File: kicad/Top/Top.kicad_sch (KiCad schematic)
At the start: 0 parts

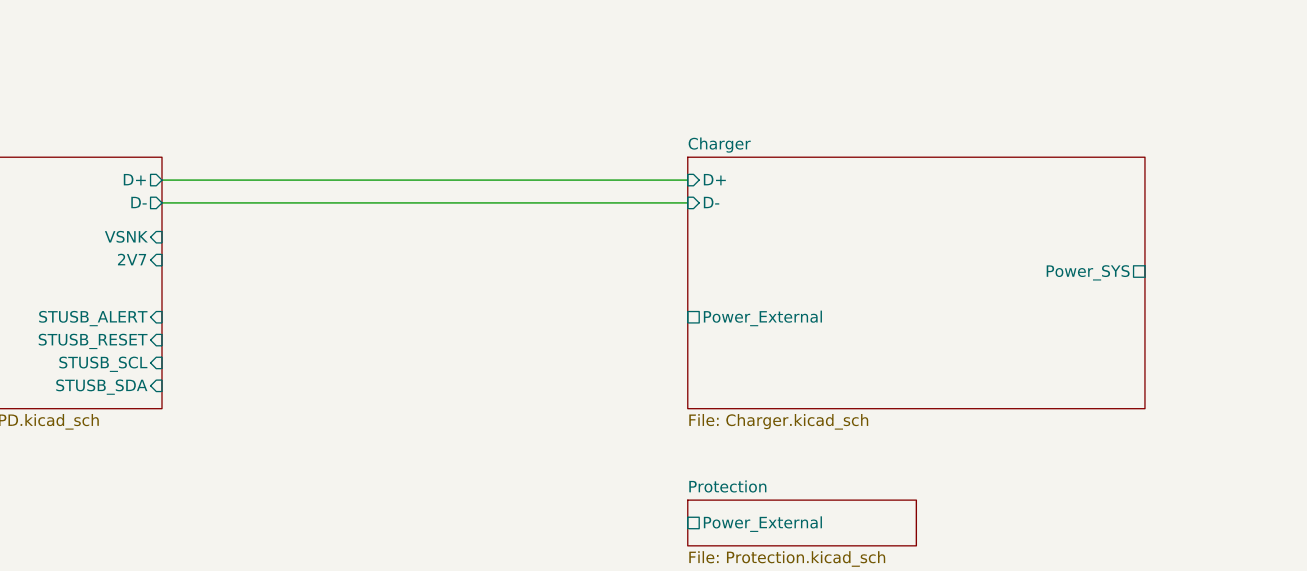
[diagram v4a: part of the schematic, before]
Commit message: Updated sheet pins for charger
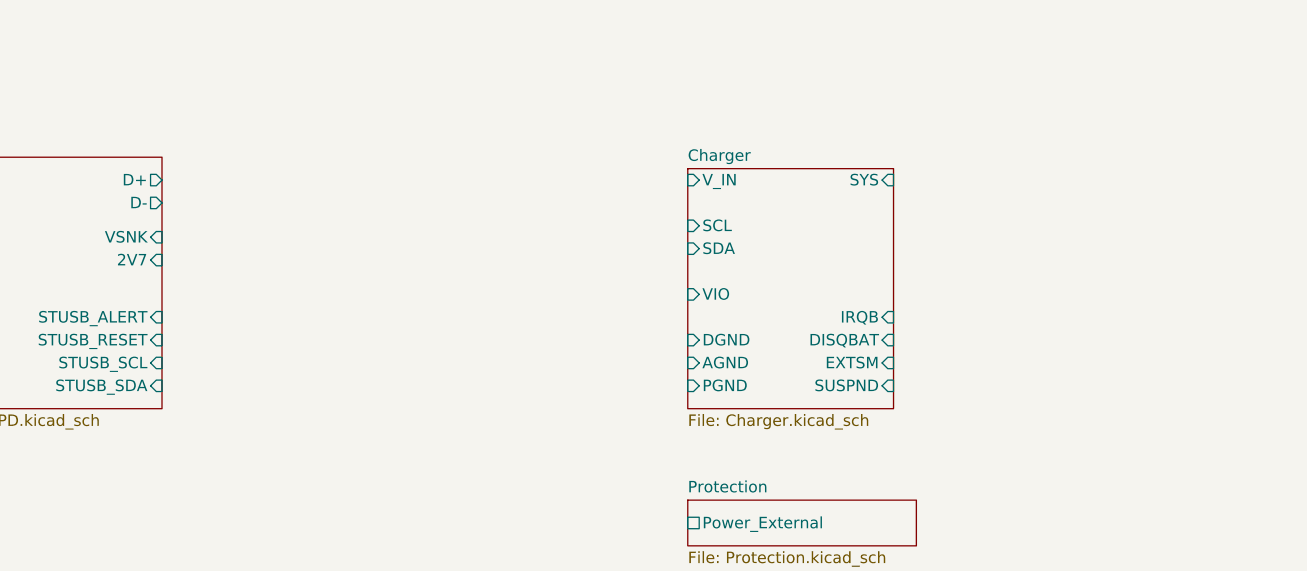
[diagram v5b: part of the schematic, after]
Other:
- sheet Charger ports: added AGND, DGND, DISQBAT, EXTSM, IRQB, PGND, SCL, SDA, SUSPND, SYS, VIO, V_IN; removed D+, D-, Power_External, Power_SYS
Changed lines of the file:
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@@
 (kicad_sch (version 20211123) (generator eeschema)
   (paper "A")
-  (wire (pts (xy 182.88 41.91) (xy 124.46 41.91))
-    (stroke (width 0.254) (type default) (color 0 0 0 0))
-  )
   (wire (pts (xy 86.36 116.84) (xy 130.81 116.84))
     (stroke (width 0) (type default) (color 0 0 0 0))
@@
   (wire (pts (xy 511.81 340.36) (xy 560.07 340.36))
     (stroke (width 0) (type default) (color 0 0 0 0))
-  )
-  (wire (pts (xy 182.88 44.45) (xy 124.46 44.45))
-    (stroke (width 0.254) (type default) (color 0 0 0 0))
   )
   (label "GND" (at 128.27 127 180)
@@
     )
   )
-  (sheet (at 182.88 39.37) (size 50.8 27.94) (fields_autoplaced)
+  (sheet (at 182.88 40.64) (size 22.86 26.67) (fields_autoplaced)
     (stroke (width 0) (type solid) (color 128 0 0 1))
     (fill (color 128 255 128 1.0000))
-    (property "Sheet name" "Charger" (id 0) (at 182.88 38.6584 0)
+    (property "Sheet name" "Charger" (id 0) (at 182.88 39.9284 0)
       (effects (font (size 1.27 1.27)) (justify left bottom))
     )
@@
       (effects (font (size 1.27 1.27)) (justify left top))
     )
-    (pin "D-" input (at 182.88 44.45 180)
+    (pin "PGND" input (at 182.88 64.77 180)
       (effects (font (size 1.27 1.27)) (justify left))
     )
-    (pin "D+" input (at 182.88 41.91 180)
+    (pin "VIO" input (at 182.88 54.61 180)
       (effects (font (size 1.27 1.27)) (justify left))
     )
-    (pin "Power_SYS" passive (at 233.68 52.07 0)
+    (pin "V_IN" input (at 182.88 41.91 180)
+      (effects (font (size 1.27 1.27)) (justify left))
+    )
+    (pin "AGND" input (at 182.88 62.23 180)
+      (effects (font (size 1.27 1.27)) (justify left))
+    )
+    (pin "DGND" input (at 182.88 59.69 180)
+      (effects (font (size 1.27 1.27)) (justify left))
+    )
+    (pin "SYS" input (at 205.74 41.91 0)
       (effects (font (size 1.27 1.27)) (justify right))
     )
-    (pin "Power_External" passive (at 182.88 57.15 180)
+    (pin "SCL" input (at 182.88 46.99 180)
       (effects (font (size 1.27 1.27)) (justify left))
     )
+    (pin "SUSPND" input (at 205.74 64.77 0)
+      (effects (font (size 1.27 1.27)) (justify right))
+    )
+    (pin "EXTSM" input (at 205.74 62.23 0)
+      (effects (font (size 1.27 1.27)) (justify right))
+    )
+    (pin "DISQBAT" input (at 205.74 59.69 0)
+      (effects (font (size 1.27 1.27)) (justify right))
+    )
+    (pin "SDA" input (at 182.88 49.53 180)
+      (effects (font (size 1.27 1.27)) (justify left))
+    )
+    (pin "IRQB" input (at 205.74 57.15 0)
+      (effects (font (size 1.27 1.27)) (justify right))
+    )
   )
